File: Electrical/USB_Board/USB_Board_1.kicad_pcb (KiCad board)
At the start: 2 copper layers, 45 x 16 mm, 22 parts, among them J1 USB_B_Mini, Q1 BC850, Q2 BC850, U1 FT232RL, U2 MFFSMF050, U3 AD8620

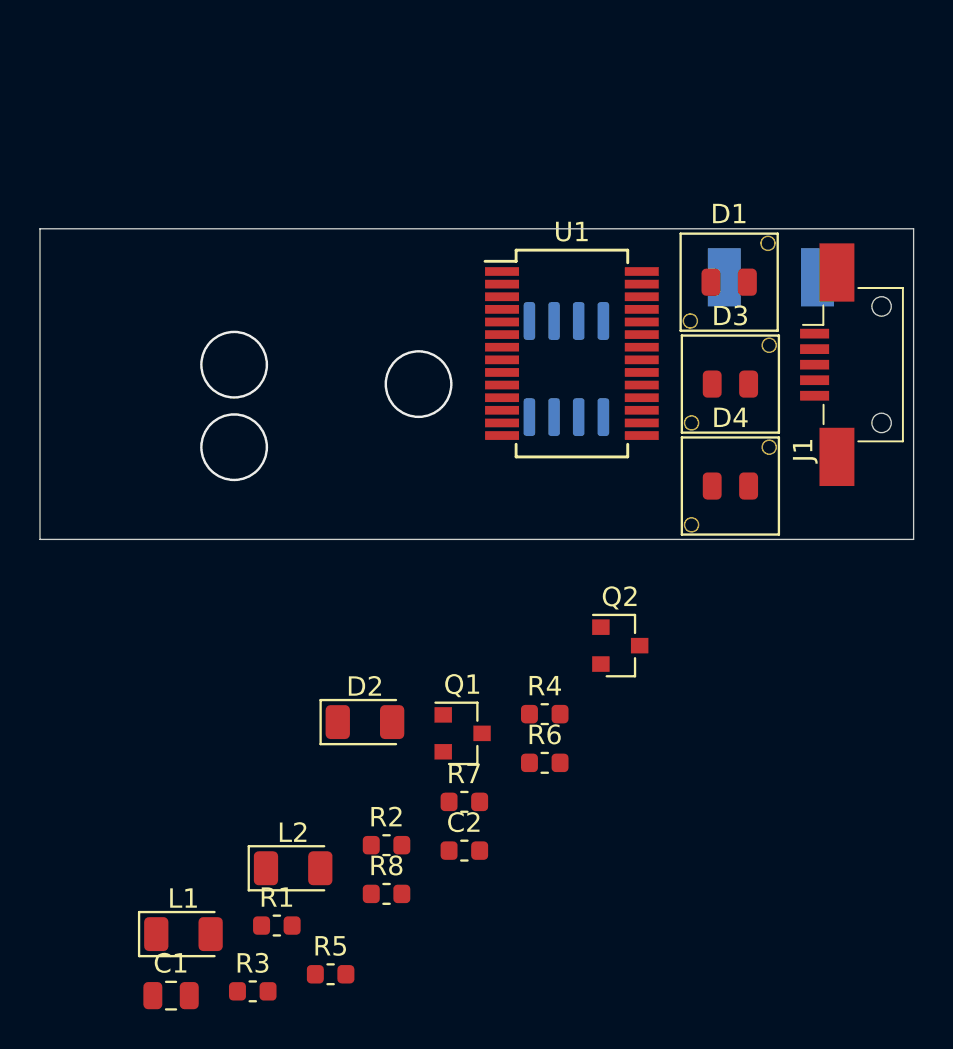
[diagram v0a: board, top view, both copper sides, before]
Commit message: Updated LED locations on USB Board.
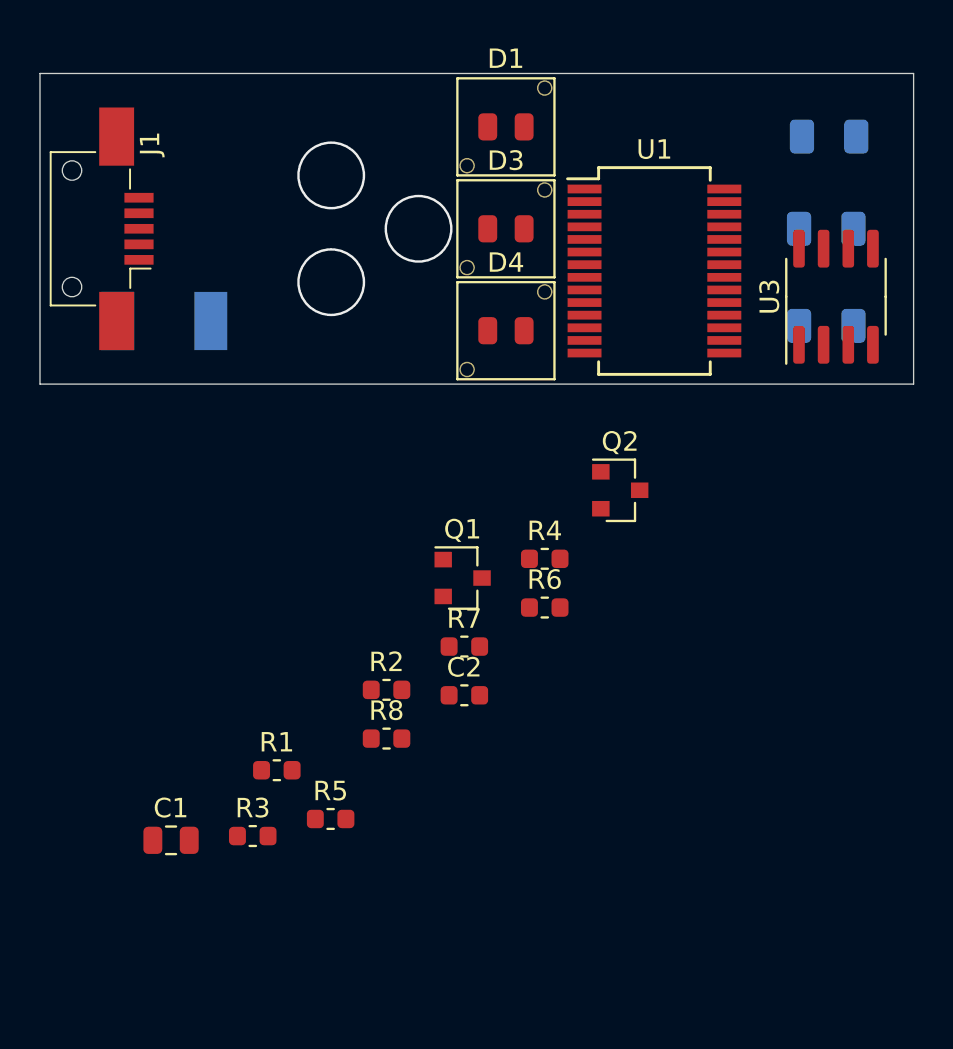
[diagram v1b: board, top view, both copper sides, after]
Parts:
- D2: value IR_PD -> PD_RX; moved to B.Cu
- L1: value IR -> IR_TX; moved to B.Cu
- L2: value IR -> IR_DTR; moved to B.Cu
- U3: moved to F.Cu
- moved L1 49.2 mm to (140.5, 100.0)
- moved L2 39.2 mm to (140.5, 105.0)
- moved J1 38.6 mm to (103.5, 100.0), turned to 180 degrees
- moved D2 38.5 mm to (140.7, 95.2)
- moved U2 36.1 mm to (104.0, 104.8), turned to 0 degrees
- moved U3 14.4 mm to (141.0, 103.5)
- moved D3 14.1 mm to (124.0, 100.0)
- moved D4 14.1 mm to (124.0, 105.2)
- moved D1 14.0 mm to (124.0, 94.8)
- moved R7 8.00 mm to (121.9, 121.5)
- moved C1 8.00 mm to (106.8, 131.5)
- moved C2 8.00 mm to (121.9, 124.0)
- moved Q1 8.00 mm to (121.8, 118.0)
- moved Q2 8.00 mm to (129.9, 113.5)
- moved R2 8.00 mm to (117.8, 123.8)
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
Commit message: Finished draft of USB board.
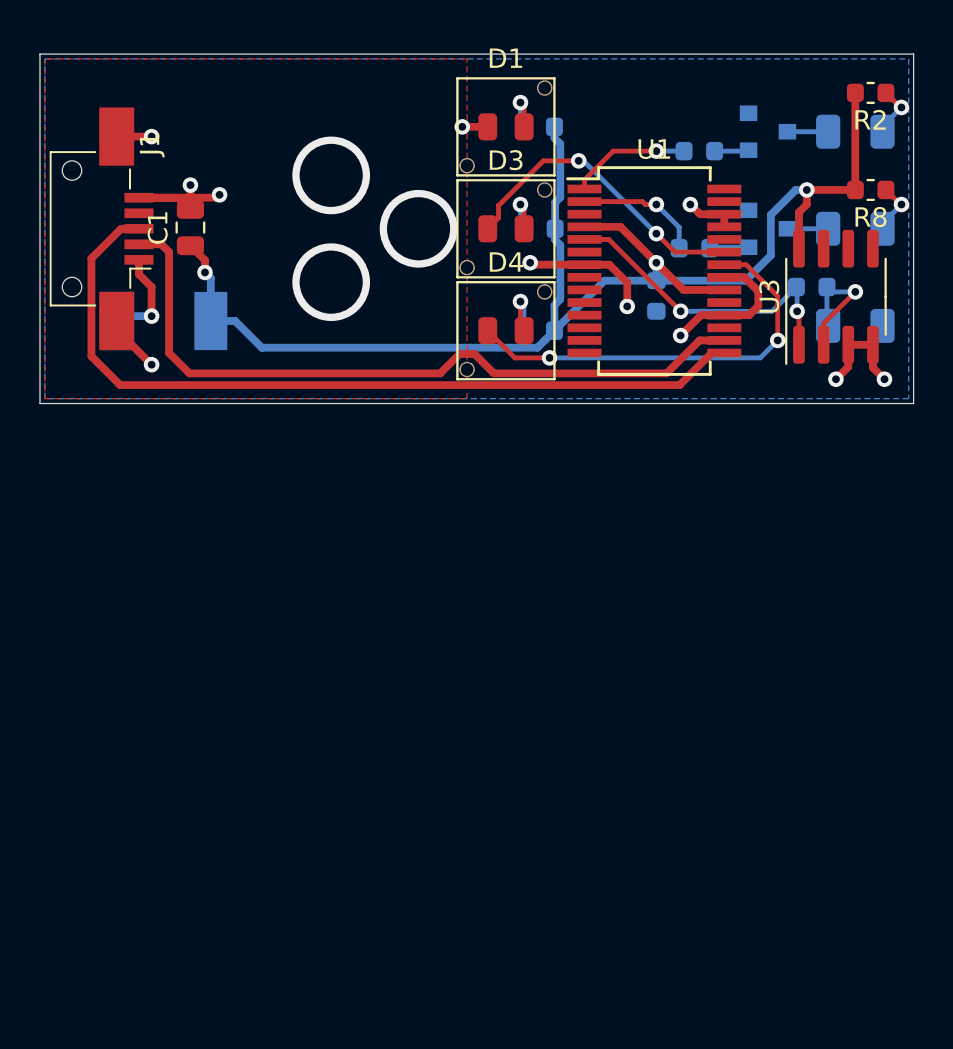
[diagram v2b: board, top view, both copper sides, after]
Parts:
- C2, Q1, Q2, R1, R3, R4, R5, R6, R7: moved to B.Cu
- moved R3 40.4 mm to (139.8, 103.0)
- moved R2 39.6 mm to (142.8, 93.0), turned to 180 degrees
- moved R8 37.7 mm to (142.8, 98.0), turned to 180 degrees
- moved R1 35.8 mm to (125.7, 94.8)
- moved R5 32.3 mm to (125.8, 100.0)
- moved C1 31.6 mm to (107.8, 99.9), turned to 90 degrees
- moved Q1 27.9 mm to (137.5, 95.0)
- moved R7 23.7 mm to (133.7, 101.0)
- moved C2 22.8 mm to (131.8, 103.5), turned to 270 degrees
- moved R4 22.5 mm to (134.0, 96.0)
- moved Q2 15.5 mm to (137.5, 100.0)
- moved R6 14.3 mm to (125.7, 105.2)
- moved D2 9.84 mm to (142.0, 105.0)
- moved L1 5.22 mm to (142.0, 95.0)
- moved L2 5.22 mm to (142.0, 100.0)
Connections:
- C1 pad 1: VBUS -> +5V
- C2 pad 1: VBUS -> +5V
- R1 pad 2: VBUS -> +5V
- U2 pad 2: VBUS -> +5V
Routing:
- net +5V: track 0.00 -> 71.3 mm, vias 0 -> 3
- net Net-(J1-Pad3): track 0.00 -> 42.0 mm
- net Net-(J1-Pad2): track 0.00 -> 37.5 mm
- net GND: track 0.00 -> 36.5 mm, vias 3 -> 14
- net Net-(D4-Pad1): track 0.00 -> 21.6 mm, vias 0 -> 2
- net Net-(R3-Pad1): track 0.00 -> 16.0 mm, vias 0 -> 2
- net Net-(D3-Pad1): track 0.00 -> 16.0 mm, vias 0 -> 2
- net Net-(D2-Pad1): track 0.00 -> 6.99 mm, vias 0 -> 1
- net /DTR: track 0.00 -> 6.50 mm, vias 0 -> 1
- net Net-(R4-Pad1): track 0.00 -> 6.21 mm, vias 0 -> 1
- net Net-(J1-Pad1): track 0.00 -> 5.02 mm, vias 0 -> 1
- net Net-(D4-Pad2): track 0.00 -> 3.15 mm, vias 0 -> 1
- net Net-(L2-Pad2): track 0.00 -> 2.76 mm, vias 0 -> 1
- net Net-(L1-Pad2): track 0.00 -> 2.76 mm, vias 0 -> 1
- net Net-(D3-Pad2): track 0.00 -> 2.67 mm, vias 0 -> 1
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- added copper zone on B.Cu, net GND
- added copper zone on F.Cu, net GND
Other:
- board size 45 x 16 mm -> 45 x 18 mm

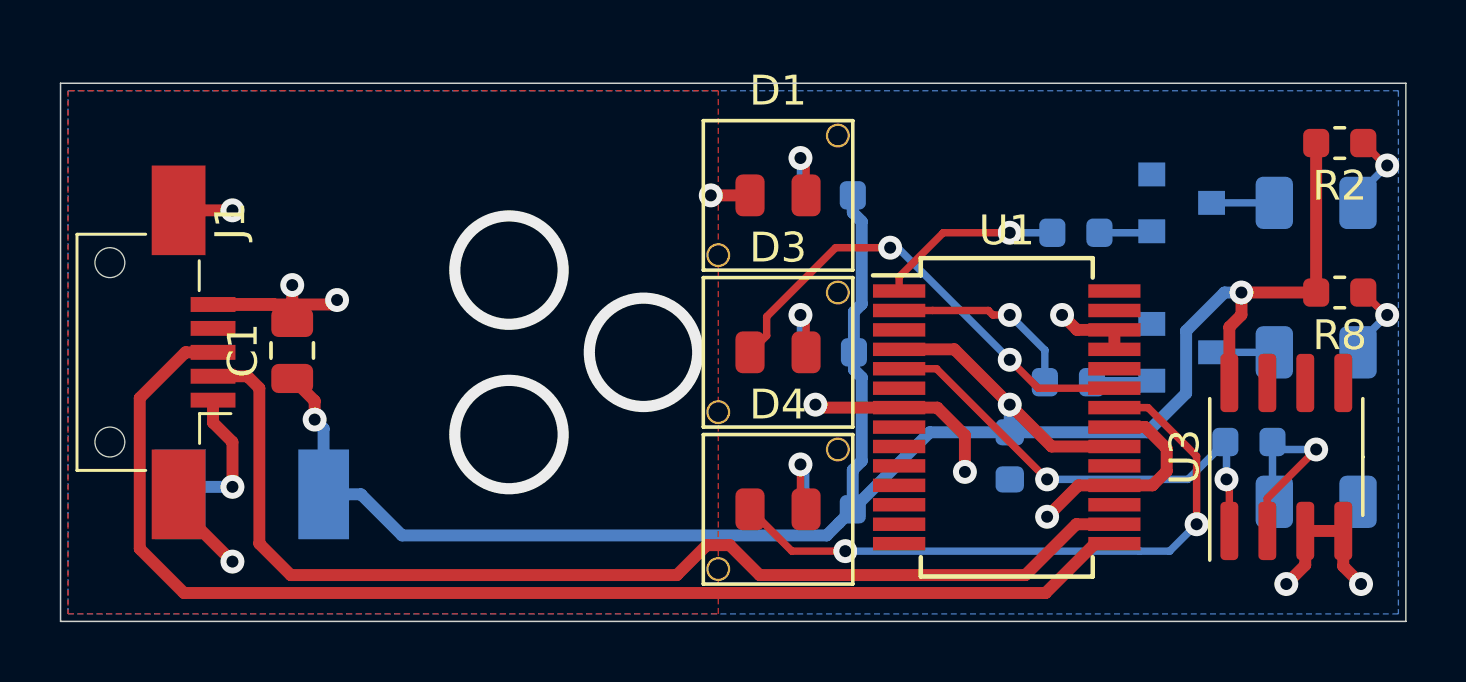
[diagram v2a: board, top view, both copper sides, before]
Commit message: Fixed layout for USB board.
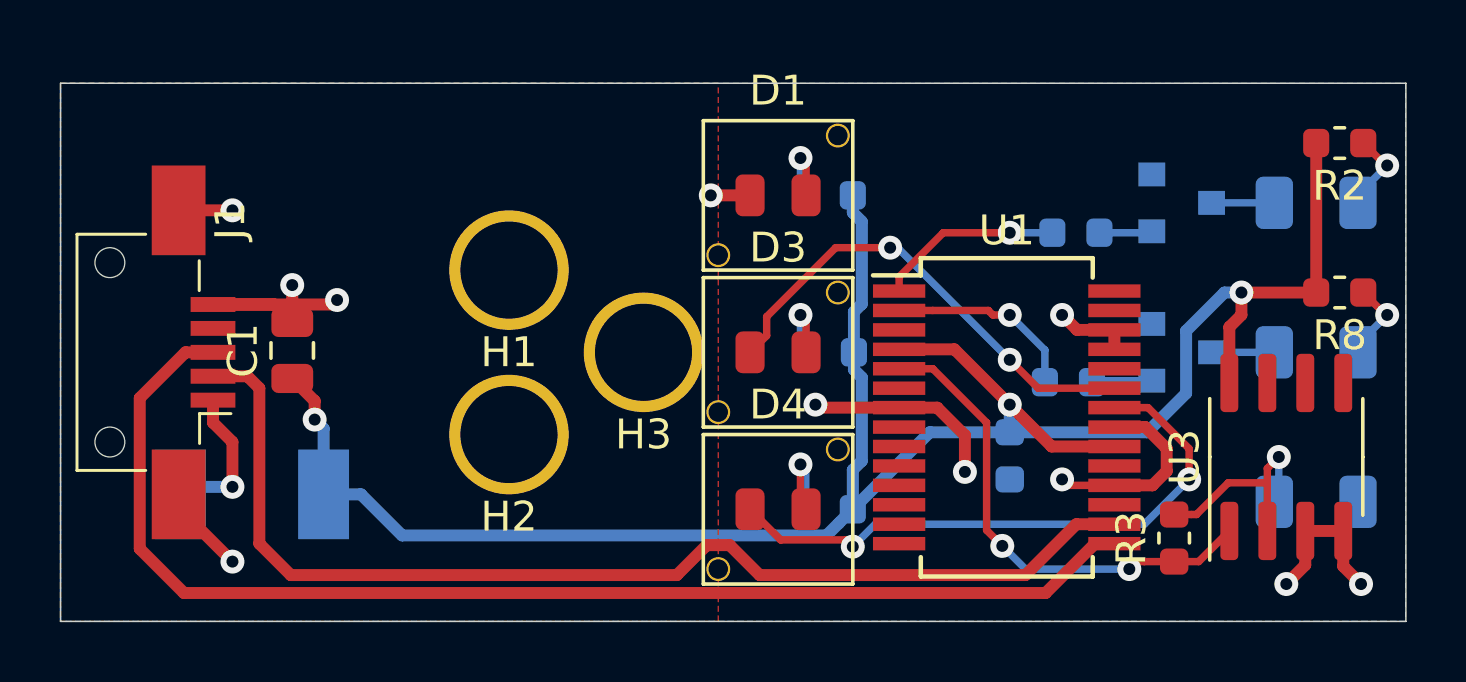
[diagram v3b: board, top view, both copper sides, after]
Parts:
- added H1: light_pipe, hodgkin:light_pipe, F.Cu at (115.0, 97.2)
- added H2: light_pipe, hodgkin:light_pipe, F.Cu at (115.0, 102.8)
- added H3: Switch, hodgkin:light_pipe, F.Cu at (119.5, 100.0)
- R3: moved to F.Cu
- moved R3 4.07 mm to (137.2, 106.2), turned to 90 degrees
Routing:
- net Net-(D4-Pad1): track 21.6 -> 20.2 mm
- net GND: track 36.5 -> 35.6 mm, vias 14 -> 11
- net Net-(D2-Pad1): track 6.99 -> 7.75 mm

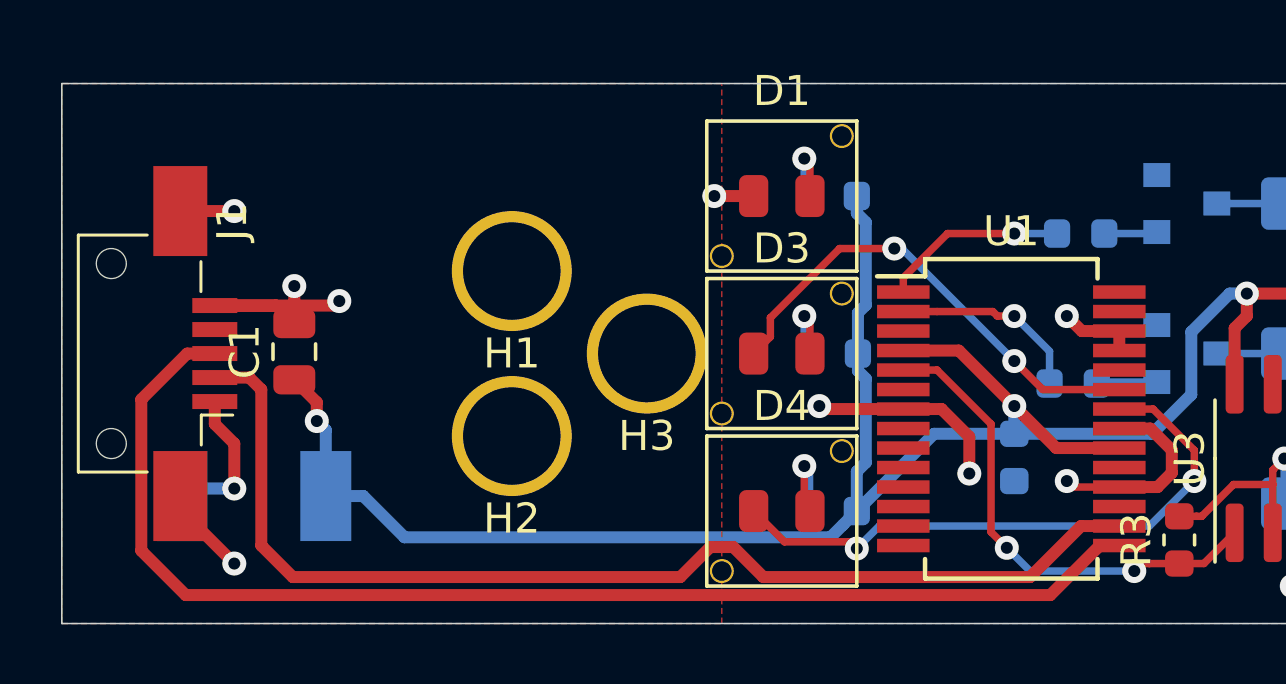
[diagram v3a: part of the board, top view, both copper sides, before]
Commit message: Finalized USB Board, inc. 3D models of light pipes.
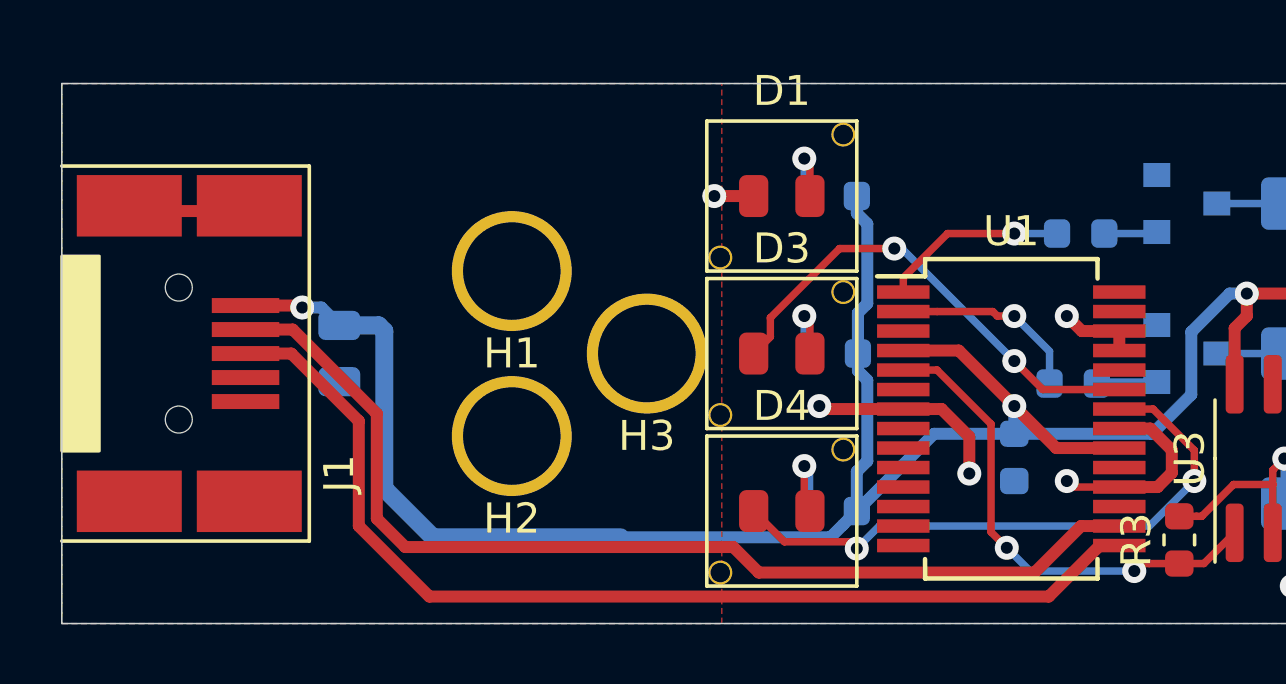
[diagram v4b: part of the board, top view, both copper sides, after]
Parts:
- removed U2: MFFSMF050, hodgkin:MF-MSMF
- C1: moved to B.Cu
- J1: footprint Connector_USB:USB_Mini-B_AdamTech_MUSB-B5-S-VT-TSMT-1_SMD_Vertical -> hodgkin:Molex_67503-1020
- moved J1 3.50 mm to (100.0, 100.0), turned to 0 degrees
- moved C1 1.50 mm to (109.2, 100.0), turned to 270 degrees
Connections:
- J1 pad 1: Net-(J1-Pad1) -> +5V
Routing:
- net GND: track 35.6 -> 24.3 mm, vias 11 -> 7
- net Net-(J1-Pad3): track 42.0 -> 35.2 mm
- net Net-(J1-Pad1): track 5.02 -> 0.00 mm, vias 1 -> 0
- net +5V: track 71.3 -> 75.5 mm
- net Net-(J1-Pad2): track 37.5 -> 35.2 mm

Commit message: Fixed part numbers on USB board.
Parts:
- removed U3: AD8620, Package_SO:SOIC-8_3.9x4.9mm_P1.27mm
- added U2: AD8620, Package_SO:SOIC-8_3.9x4.9mm_P1.27mm, F.Cu at (141.0, 103.6)
- renumbered C2 to C1, C1 to C2, D2 to D1, D1 to L1, D3 to L2, D4 to L3, L1 to L4, L2 to L5, R3 to R1, R8 to R3, R7 to R5, R1 to R6, R5 to R7, R6 to R8

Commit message: changed LED and PD footprints on USB boards
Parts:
- R4, R5: value R -> 4.7k
